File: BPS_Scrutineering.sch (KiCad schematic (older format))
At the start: 22 parts, among them J1 Conn_01x01_Female, J10 Conn_01x01_Female, J11 Conn_01x01_Female, J12 Conn_01x01_Female, J13 Conn_01x01_Female, J14 Conn_01x01_Female, J2 Conn_01x01_Female, J3 Conn_01x01_Female, J4 Conn_01x01_Female, J5 Conn_01x01_Female, J6 Conn_01x01_Female, J7 Conn_01x01_Female, J8 Conn_01x01_Female, J9 Conn_01x01_Female, SW1 SW_DIP_x07, SW2 SW_DIP_x07

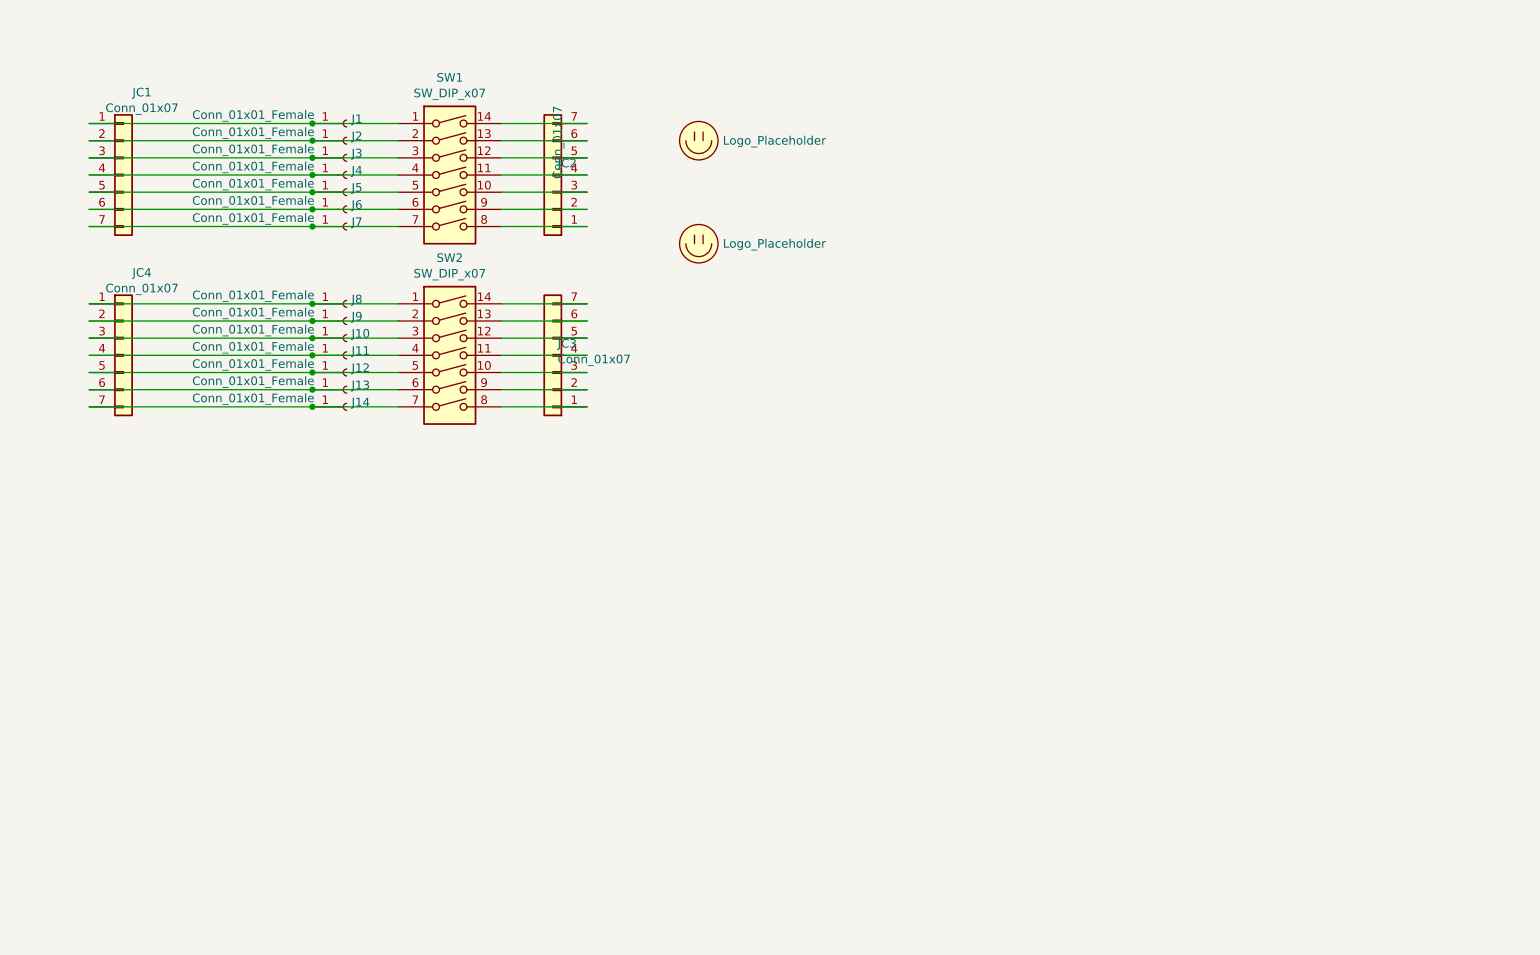
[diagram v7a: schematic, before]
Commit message: Fix issues with connector sizes and wiring
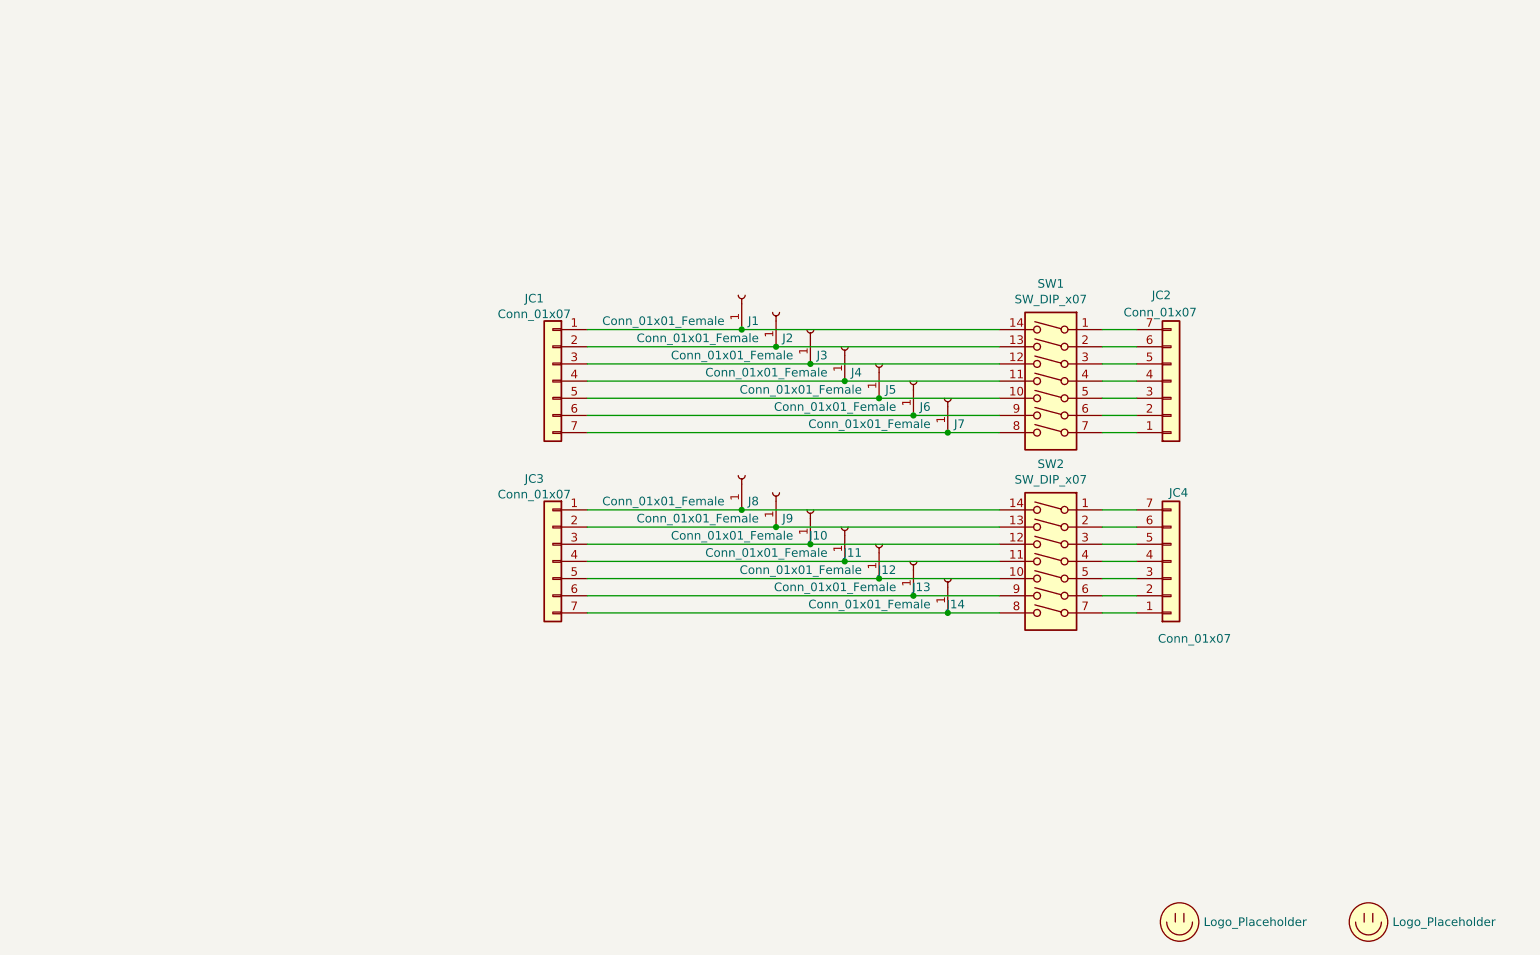
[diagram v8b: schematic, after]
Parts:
- renumbered JC4 to JC3, JC3 to JC4
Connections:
- net at J1.1 (Pin_1), JC1.1 (Pin_1): now also SW1.14; no longer SW1.1
- net at J2.1 (Pin_1), JC1.2 (Pin_2): now also SW1.13; no longer SW1.2
- net at J3.1 (Pin_1), JC1.3 (Pin_3): now also SW1.12; no longer SW1.3
- net at J4.1 (Pin_1), JC1.4 (Pin_4): now also SW1.11; no longer SW1.4
- net at J5.1 (Pin_1), JC1.5 (Pin_5): now also SW1.10; no longer SW1.5
- net at J6.1 (Pin_1), JC1.6 (Pin_6): now also SW1.9; no longer SW1.6
- net at J7.1 (Pin_1), JC1.7 (Pin_7): now also SW1.8; no longer SW1.7
- net at J8.1 (Pin_1), JC3.1 (Pin_1): now also SW2.14; no longer SW2.1
- net at J9.1 (Pin_1), JC3.2 (Pin_2): now also SW2.13; no longer SW2.2
- net at J10.1 (Pin_1), JC3.3 (Pin_3): now also SW2.12; no longer SW2.3
- net at J11.1 (Pin_1), JC3.4 (Pin_4): now also SW2.11; no longer SW2.4
- net at J12.1 (Pin_1), JC3.5 (Pin_5): now also SW2.10; no longer SW2.5
- net at J13.1 (Pin_1), JC3.6 (Pin_6): now also SW2.9; no longer SW2.6
- net at J14.1 (Pin_1), JC3.7 (Pin_7): now also SW2.8; no longer SW2.7
- net at JC2.1 (Pin_1): now also SW1.7; no longer SW1.8
- net at JC2.2 (Pin_2): now also SW1.6; no longer SW1.9
- net at JC2.3 (Pin_3): now also SW1.5; no longer SW1.10
- net at JC2.4 (Pin_4): now also SW1.4; no longer SW1.11
- net at JC2.5 (Pin_5): now also SW1.3; no longer SW1.12
- net at JC2.6 (Pin_6): now also SW1.2; no longer SW1.13
- net at JC2.7 (Pin_7): now also SW1.1; no longer SW1.14
- net at JC4.1 (Pin_1): now also SW2.7; no longer SW2.8
- net at JC4.2 (Pin_2): now also SW2.6; no longer SW2.9
- net at JC4.3 (Pin_3): now also SW2.5; no longer SW2.10
- net at JC4.4 (Pin_4): now also SW2.4; no longer SW2.11
- net at JC4.5 (Pin_5): now also SW2.3; no longer SW2.12
- net at JC4.6 (Pin_6): now also SW2.2; no longer SW2.13
- net at JC4.7 (Pin_7): now also SW2.1; no longer SW2.14
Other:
- moved on the sheet: J1, J2, JC1, JC2, JC3, JC4, SW1, SW2
